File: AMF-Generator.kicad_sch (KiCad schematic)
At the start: 27 parts, among them J1 SW_OUT, J2 CUR_SENSE, J3 PWR_IN, Q1 ISC012N04LM6ATMA1, Q2 ISC012N04LM6ATMA1, U1 ACS732KLATR-75AB, U2 UCC21540

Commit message: initial pass of layout complete
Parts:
- added D3: LED, LED_SMD:LED_0805_2012Metric, symbol Device:LED
- added R9: 2K, Resistor_SMD:R_0805_2012Metric, symbol Device:R
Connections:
- net +12V: now also R9.1
- net GNDPWR: now also D3.1 (K)
- net SW_A: now reaches D1.5, D1.6, D1.7, D1.8, J1.1 (Pin_1), Q1.5 (D), R6.1
- net SW_B: now reaches D2.5, D2.6, D2.7, D2.8, J1.2 (Pin_2), Q2.5 (D), R7.1
- net AC_B: now reaches J2.1 (Pin_1), U1.5 (IP-), U1.6 (IP-), U1.7 (IP-), U1.8 (IP-)
- net AC_A: now reaches J2.2 (Pin_2), U1.1 (IP+), U1.2 (IP+), U1.3 (IP+), U1.4 (IP+)
- net SWA renamed PWM_A
- net SWB renamed PWM_B
- new net: D3.2 (A), R9.2
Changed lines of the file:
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@@
     (effects (font (size 1.27 1.27)) (justify left bottom))
+  )
+  (global_label "AC_A" (shape input) (at 218.44 107.95 90) (fields_autoplaced)
+    (effects (font (size 1.27 1.27)) (justify left))
+    (property "Intersheetrefs" "${INTERSHEET_REFS}" (at 218.44 100.6294 90)
+      (effects (font (size 1.27 1.27)) (justify left) hide)
+    )
+  )
+  (global_label "SW_A" (shape input) (at 175.895 59.69 90) (fields_autoplaced)
+    (effects (font (size 1.27 1.27)) (justify left))
+    (property "Intersheetrefs" "${INTERSHEET_REFS}" (at 175.895 52.0671 90)
+      (effects (font (size 1.27 1.27)) (justify left) hide)
+    )
   )
   (global_label "FAULT" (shape input) (at 274.955 110.49 0) (fields_autoplaced)
@@
     )
   )
-  (global_label "SWA" (shape input) (at 59.69 87.63 180) (fields_autoplaced)
+  (global_label "PWM_A" (shape input) (at 59.69 87.63 180) (fields_autoplaced)
     (effects (font (size 1.27 1.27)) (justify right))
-    (property "Intersheetrefs" "${INTERSHEET_REFS}" (at 53.0347 87.63 0)
+    (property "Intersheetrefs" "${INTERSHEET_REFS}" (at 50.5552 87.63 0)
       (effects (font (size 1.27 1.27)) (justify right) hide)
     )
   )
-  (global_label "SWB" (shape input) (at 59.69 90.17 180) (fields_autoplaced)
+  (global_label "AC_B" (shape input) (at 218.44 113.03 270) (fields_autoplaced)
     (effects (font (size 1.27 1.27)) (justify right))
-    (property "Intersheetrefs" "${INTERSHEET_REFS}" (at 52.8533 90.17 0)
+    (property "Intersheetrefs" "${INTERSHEET_REFS}" (at 218.44 120.532 90)
+      (effects (font (size 1.27 1.27)) (justify right) hide)
+    )
+  )
+  (global_label "PWM_B" (shape input) (at 59.69 90.17 180) (fields_autoplaced)
+    (effects (font (size 1.27 1.27)) (justify right))
+    (property "Intersheetrefs" "${INTERSHEET_REFS}" (at 50.3738 90.17 0)
+      (effects (font (size 1.27 1.27)) (justify right) hide)
+    )
+  )
+  (global_label "SW_B" (shape input) (at 176.53 77.47 270) (fields_autoplaced)
+    (effects (font (size 1.27 1.27)) (justify right))
+    (property "Intersheetrefs" "${INTERSHEET_REFS}" (at 176.53 85.2743 90)
       (effects (font (size 1.27 1.27)) (justify right) hide)
     )
@@
         (path "/c3df021c-646c-4a68-ac14-a081c2121d02"
           (reference "C22") (unit 1)
+        )
+      )
+    )
+  )
+  (symbol (lib_id "power:+12V") (at 31.115 32.385 0) (unit 1)
+    (in_bom yes) (on_board yes) (dnp no) (fields_autoplaced)
+    (property "Reference" "#PWR069" (at 31.115 36.195 0)
+      (effects (font (size 1.27 1.27)) hide)
+    )
+    (property "Value" "+12V" (at 31.115 29.21 0)
+      (effects (font (size 1.27 1.27)))
+    )
+    (property "Footprint" "" (at 31.115 32.385 0)
+      (effects (font (size 1.27 1.27)) hide)
+    )
+    (property "Datasheet" "" (at 31.115 32.385 0)
+      (effects (font (size 1.27 1.27)) hide)
+    )
+    (pin "1")
+    (instances
+      (project "AMF-Generator"
+        (path "/c3df021c-646c-4a68-ac14-a081c2121d02"
+          (reference "#PWR069") (unit 1)
         )
       )
@@
     )
   )
+  (symbol (lib_id "power:GNDPWR") (at 31.115 47.625 0) (unit 1)
+    (in_bom yes) (on_board yes) (dnp no) (fields_autoplaced)
+    (property "Reference" "#PWR068" (at 31.115 52.705 0)
+      (effects (font (size 1.27 1.27)) hide)
+    )
+    (property "Value" "GNDPWR" (at 30.988 52.07 0)
+      (effects (font (size 1.27 1.27)))
+    )
+    (property "Footprint" "" (at 31.115 48.895 0)
+      (effects (font (size 1.27 1.27)) hide)
+    )
+    (property "Datasheet" "" (at 31.115 48.895 0)
+      (effects (font (size 1.27 1.27)) hide)
+    )
+    (pin "1")
+    (instances
+      (project "AMF-Generator"
+        (path "/c3df021c-646c-4a68-ac14-a081c2121d02"
+          (reference "#PWR068") (unit 1)
+        )
+      )
+    )
+  )
   (symbol (lib_id "power:+12V") (at 50.8 39.37 180) (unit 1)
     (in_bom yes) (on_board yes) (dnp no)
@@
         (path "/c3df021c-646c-4a68-ac14-a081c2121d02"
           (reference "C36") (unit 1)
+        )
+      )
+    )
+  )
+  (symbol (lib_id "Device:LED") (at 31.115 43.815 90) (unit 1)
+    (in_bom yes) (on_board yes) (dnp no) (fields_autoplaced)
+    (property "Reference" "D3" (at 34.29 44.7675 90)
+      (effects (font (size 1.27 1.27)) (justify right))
+    )
+    (property "Value" "LED" (at 34.29 47.3075 90)
+      (effects (font (size 1.27 1.27)) (justify right))
+    )
+    (property "Footprint" "LED_SMD:LED_0805_2012Metric" (at 31.115 43.815 0)
+      (effects (font (size 1.27 1.27)) hide)
+    )
+    (property "Datasheet" "~" (at 31.115 43.815 0)
+      (effects (font (size 1.27 1.27)) hide)
+    )
+    (pin "1")
+    (pin "2")
+    (instances
+      (project "AMF-Generator"
+        (path "/c3df021c-646c-4a68-ac14-a081c2121d02"
+          (reference "D3") (unit 1)
         )
       )
@@
         )
       )
+    )
+  )
+  (symbol (lib_id "Device:R") (at 31.115 36.195 0) (unit 1)
+    (in_bom yes) (on_board yes) (dnp no) (fields_autoplaced)
+    (property "Reference" "R9" (at 33.02 35.56 0)
+      (effects (font (size 1.27 1.27)) (justify left))
+    )
+    (property "Value" "2K" (at 33.02 38.1 0)
+      (effects (font (size 1.27 1.27)) (justify left))
+    )
+    (property "Footprint" "Resistor_SMD:R_0805_2012Metric" (at 29.337 36.195 90)
+      (effects (font (size 1.27 1.27)) hide)
+    )
+    (property "Datasheet" "~" (at 31.115 36.195 0)
+      (effects (font (size 1.27 1.27)) hide)
+    )
+    (pin "1")
+    (pin "2")
+    (instances
+      (project "AMF-Generator"
+        (path "/c3df021c-646c-4a68-ac14-a081c2121d02"
+          (reference "R9") (unit 1)
+        )
+      )

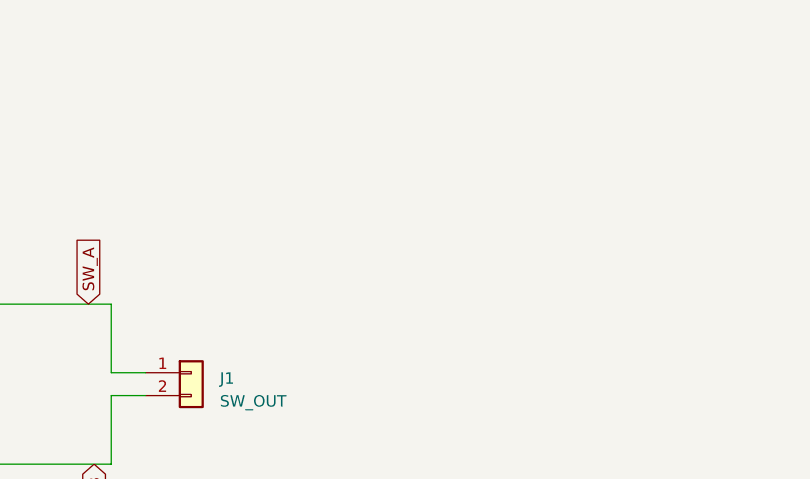
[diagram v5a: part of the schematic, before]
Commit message: Cleanup, changed board outline, DRC errors resolved
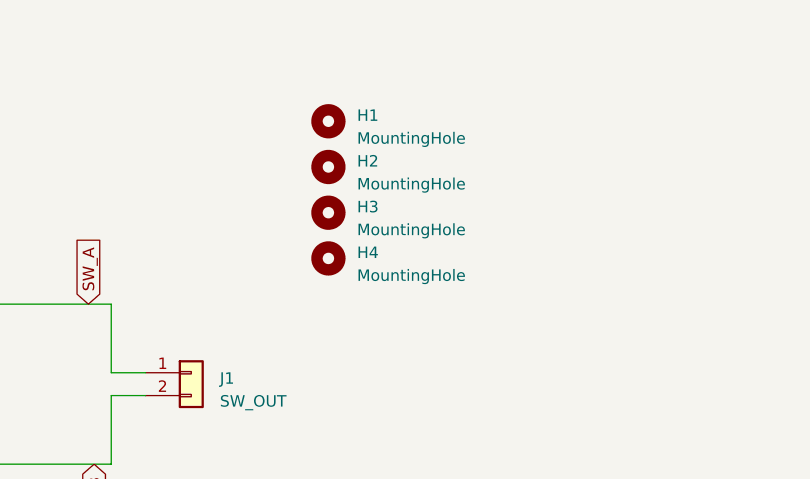
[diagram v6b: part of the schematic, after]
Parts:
- added H1, H2, H3, H4: MountingHole, MountingHole:MountingHole_3.2mm_M3_ISO7380_Pad, symbol Mechanical:MountingHole
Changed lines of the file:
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@@
+    )
+  )
+  (symbol (lib_id "Mechanical:MountingHole") (at 202.565 44.45 0) (unit 1)
+    (in_bom yes) (on_board yes) (dnp no) (fields_autoplaced)
+    (property "Reference" "H2" (at 205.74 43.815 0)
+      (effects (font (size 1.27 1.27)) (justify left))
+    )
+    (property "Value" "MountingHole" (at 205.74 46.355 0)
+      (effects (font (size 1.27 1.27)) (justify left))
+    )
+    (property "Footprint" "MountingHole:MountingHole_3.2mm_M3_ISO7380_Pad" (at 202.565 44.45 0)
+      (effects (font (size 1.27 1.27)) hide)
+    )
+    (property "Datasheet" "~" (at 202.565 44.45 0)
+      (effects (font (size 1.27 1.27)) hide)
+    )
+    (instances
+      (project "AMF-Generator"
+        (path "/c3df021c-646c-4a68-ac14-a081c2121d02"
+          (reference "H2") (unit 1)
+        )
+      )
     )
   )
@@
         (path "/c3df021c-646c-4a68-ac14-a081c2121d02"
           (reference "#PWR015") (unit 1)
+        )
+      )
+    )
+  )
+  (symbol (lib_id "Mechanical:MountingHole") (at 202.565 54.61 0) (unit 1)
+    (in_bom yes) (on_board yes) (dnp no) (fields_autoplaced)
+    (property "Reference" "H4" (at 205.74 53.975 0)
+      (effects (font (size 1.27 1.27)) (justify left))
+    )
+    (property "Value" "MountingHole" (at 205.74 56.515 0)
+      (effects (font (size 1.27 1.27)) (justify left))
+    )
+    (property "Footprint" "MountingHole:MountingHole_3.2mm_M3_ISO7380_Pad" (at 202.565 54.61 0)
+      (effects (font (size 1.27 1.27)) hide)
+    )
+    (property "Datasheet" "~" (at 202.565 54.61 0)
+      (effects (font (size 1.27 1.27)) hide)
+    )
+    (instances
+      (project "AMF-Generator"
+        (path "/c3df021c-646c-4a68-ac14-a081c2121d02"
+          (reference "H4") (unit 1)
         )
       )
@@
         (path "/c3df021c-646c-4a68-ac14-a081c2121d02"
           (reference "#PWR011") (unit 1)
+        )
+      )
+    )
+  )
+  (symbol (lib_id "Mechanical:MountingHole") (at 202.565 39.37 0) (unit 1)
+    (in_bom yes) (on_board yes) (dnp no) (fields_autoplaced)
+    (property "Reference" "H1" (at 205.74 38.735 0)
+      (effects (font (size 1.27 1.27)) (justify left))
+    )
+    (property "Value" "MountingHole" (at 205.74 41.275 0)
+      (effects (font (size 1.27 1.27)) (justify left))
+    )
+    (property "Footprint" "MountingHole:MountingHole_3.2mm_M3_ISO7380_Pad" (at 202.565 39.37 0)
+      (effects (font (size 1.27 1.27)) hide)
+    )
+    (property "Datasheet" "~" (at 202.565 39.37 0)
+      (effects (font (size 1.27 1.27)) hide)
+    )
+    (instances
+      (project "AMF-Generator"
+        (path "/c3df021c-646c-4a68-ac14-a081c2121d02"
+          (reference "H1") (unit 1)
         )
       )
@@
         )
       )
+    )
+  )
+  (symbol (lib_id "Mechanical:MountingHole") (at 202.565 49.53 0) (unit 1)
+    (in_bom yes) (on_board yes) (dnp no) (fields_autoplaced)
+    (property "Reference" "H3" (at 205.74 48.895 0)
+      (effects (font (size 1.27 1.27)) (justify left))
+    )
+    (property "Value" "MountingHole" (at 205.74 51.435 0)
+      (effects (font (size 1.27 1.27)) (justify left))
+    )
+    (property "Footprint" "MountingHole:MountingHole_3.2mm_M3_ISO7380_Pad" (at 202.565 49.53 0)
+      (effects (font (size 1.27 1.27)) hide)
+    )
+    (property "Datasheet" "~" (at 202.565 49.53 0)
+      (effects (font (size 1.27 1.27)) hide)
+    )
+    (instances
+      (project "AMF-Generator"
+        (path "/c3df021c-646c-4a68-ac14-a081c2121d02"
+          (reference "H3") (unit 1)
+        )
+      )

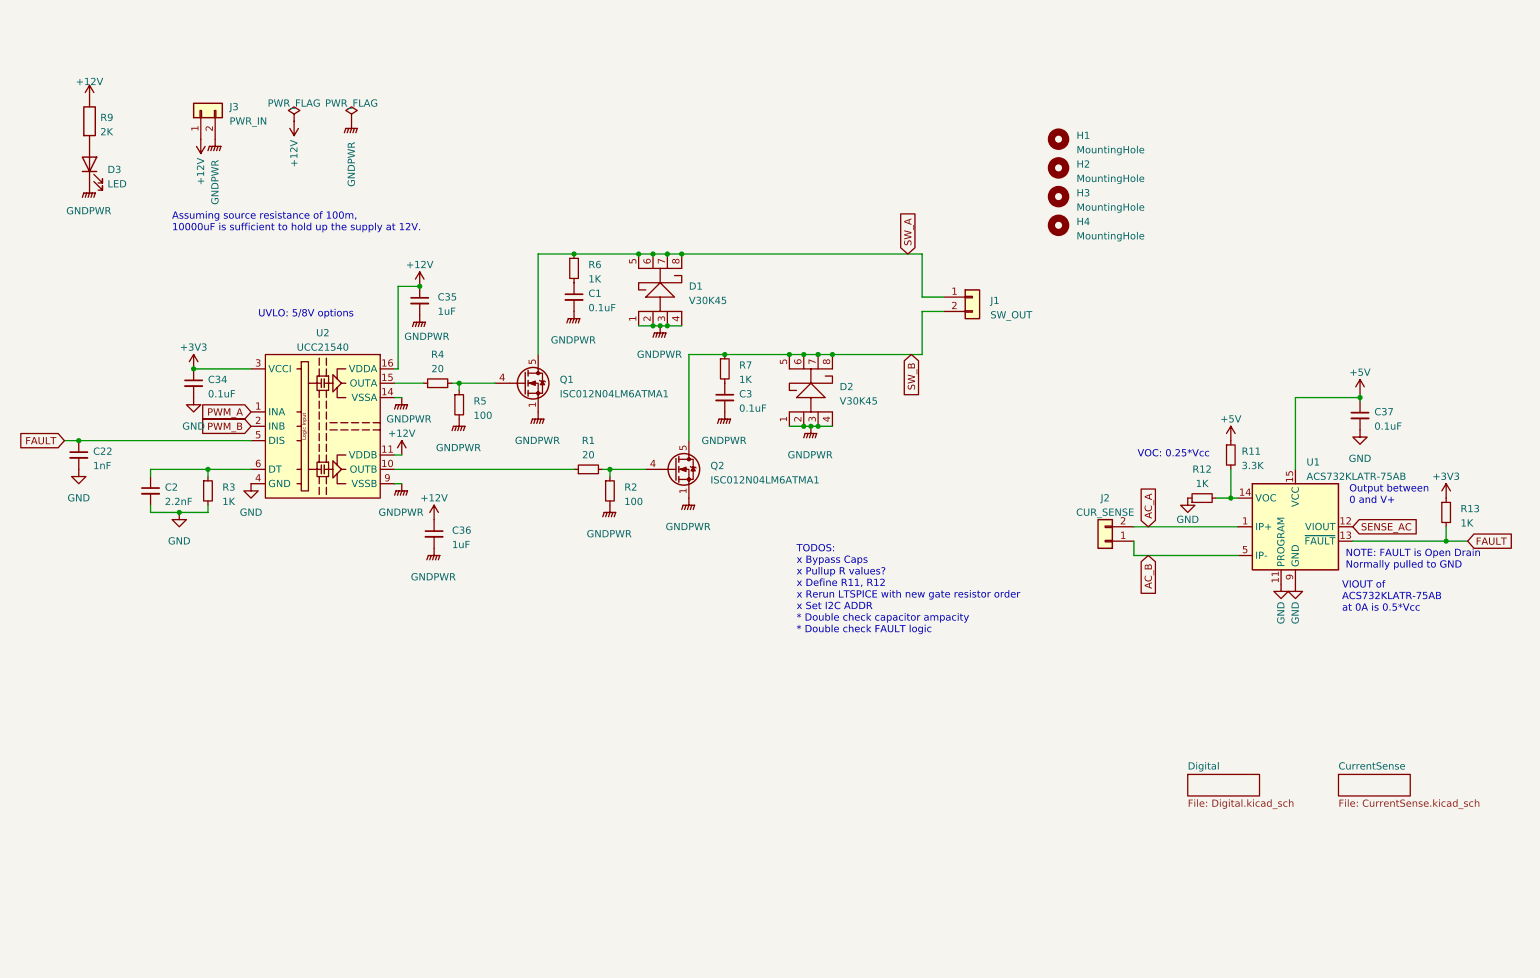
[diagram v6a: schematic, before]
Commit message: Fix schematic issues (incl QTPY symbol) and some board cleanup
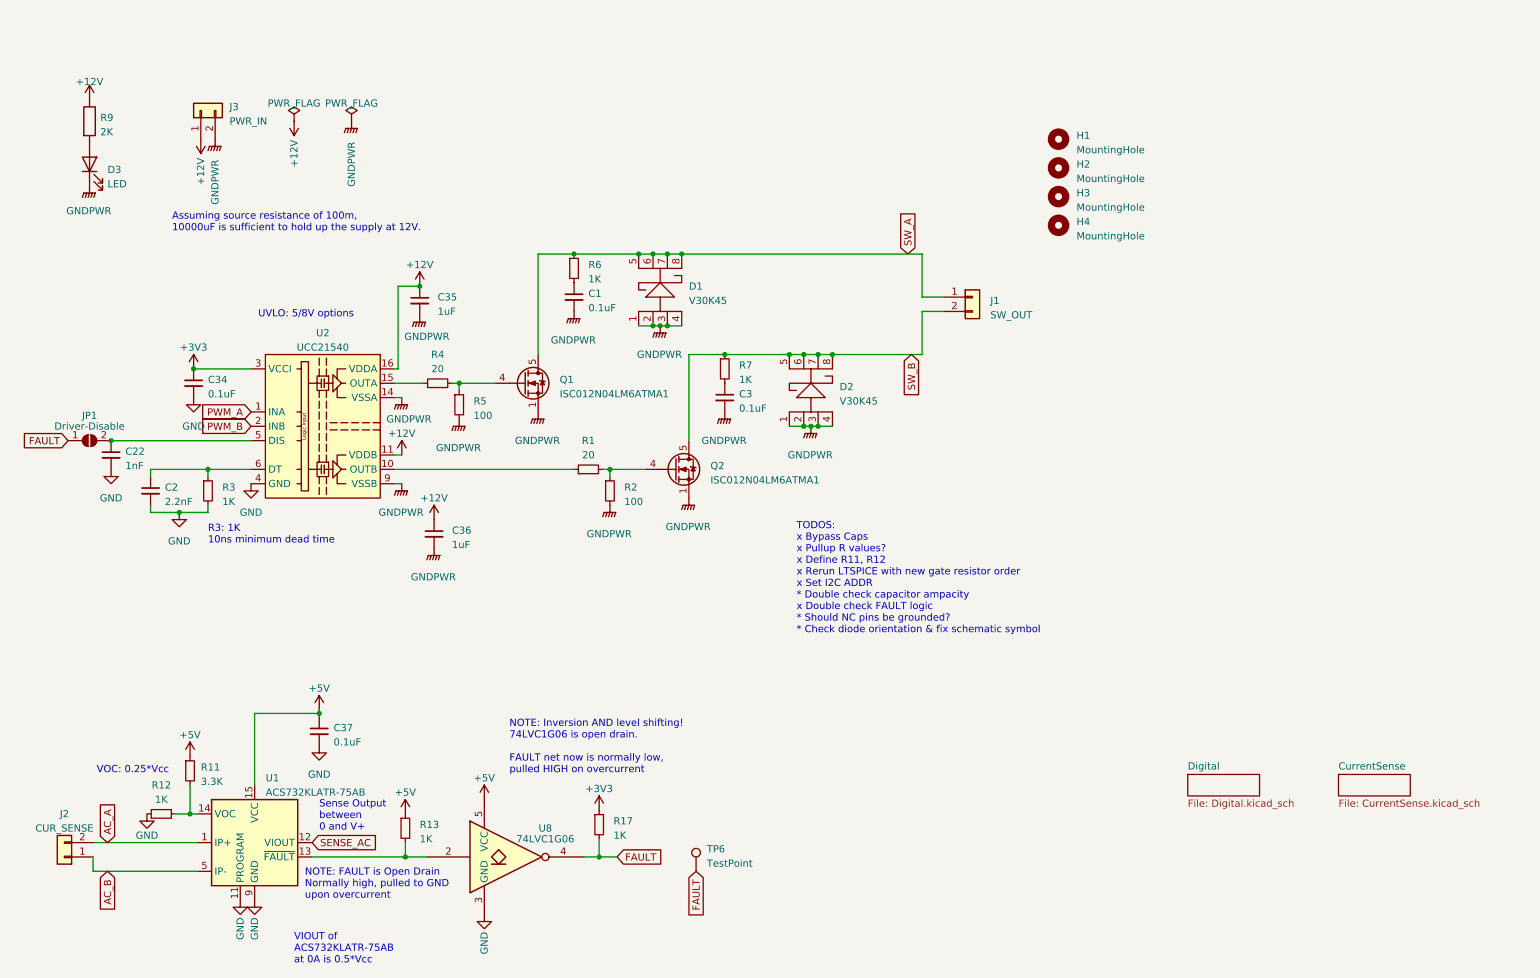
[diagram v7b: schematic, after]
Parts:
- added JP1: Driver-Disable, Jumper:SolderJumper-2_P1.3mm_Open_RoundedPad1.0x1.5mm, symbol Jumper:SolderJumper_2_Open
- added R17: 1K, Resistor_SMD:R_0805_2012Metric, symbol Device:R_Small
- added TP6: TestPoint, TestPoint:TestPoint_THTPad_D2.0mm_Drill1.0mm, symbol Connector:TestPoint
- added U8: 74LVC1G06, Package_TO_SOT_SMD:SOT-23-5_HandSoldering, symbol 74xGxx:74LVC1G06
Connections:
- net +3V3: now also R17.1; no longer R13.1
- net +5V: now also R13.1, U8.5 (VCC)
- net FAULT: now also JP1.1 (A), R17.2, TP6.1, U8.4; no longer C22.1, R13.2, U1.13 (~{FAULT}), U2.5 (DIS)
- net GND: now also U8.3 (GND)
- new net: C22.1, JP1.2 (B), U2.5 (DIS)
- new net: R13.2, U1.13 (~{FAULT}), U8.2
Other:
- note added: "NOTE: FAULT is Open Drain Normally high, pulled to GND upon overcurrent"
- note added: "NOTE: Inversion AND level shifting! 74LVC1G06 is open drain. FAULT net now is normally low, pulled HIGH on overcurrent"
- note added: "R3: 1K 10ns minimum dead time"
- note added: "Sense Output between 0 and V+"
- note added: "TODOS: x Bypass Caps x Pullup R values? x Define R11, R12 x Rerun LTSPICE with new gate resistor order x Set I2C ADDR * Double check capacitor ampacity x Double check FAULT logic * Should NC pins be grounded? * Check diode orientation & fix schematic symbol"
- note removed: "NOTE: FAULT is Open Drain Normally pulled to GND"
- note removed: "Output between 0 and V+"
- note removed: "TODOS: x Bypass Caps x Pullup R values? x Define R11, R12 x Rerun LTSPICE with new gate resistor order x Set I2C ADDR * Double check capacitor ampacity * Double check FAULT logic"
- moved on the sheet: C22, C37, J2, R11, R12, R13, U1

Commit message: misc changes
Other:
- note added: "TODOS: x Bypass Caps x Pullup R values? x Define R11, R12 x Rerun LTSPICE with new gate resistor order x Set I2C ADDR * Double check capacitor ampacity x Double check FAULT logic * Should NC pins be grounded? * Check diode orientation & fix schematic symbol * Calculate appropriate gate resistor value - 20 may be too high"
- note removed: "TODOS: x Bypass Caps x Pullup R values? x Define R11, R12 x Rerun LTSPICE with new gate resistor order x Set I2C ADDR * Double check capacitor ampacity x Double check FAULT logic * Should NC pins be grounded? * Check diode orientation & fix schematic symbol"
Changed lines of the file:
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@@
     (effects (font (size 1.27 1.27)) (justify left bottom))
   )
-  (text "TODOS:\nx Bypass Caps\nx Pullup R values?\nx Define R11, R12\nx Rerun LTSPICE with new gate resistor order\nx Set I2C ADDR\n* Double check capacitor ampacity\nx Double check FAULT logic\n* Should NC pins be grounded?\n* Check diode orientation & fix schematic symbol"
+  (text "TODOS:\nx Bypass Caps\nx Pullup R values?\nx Define R11, R12\nx Rerun LTSPICE with new gate resistor order\nx Set I2C ADDR\n* Double check capacitor ampacity\nx Double check FAULT logic\n* Should NC pins be grounded?\n* Check diode orientation & fix schematic symbol\n* Calculate appropriate gate resistor value - 20 may be too high"
     (at 156.21 127 0)
     (effects (font (size 1.27 1.27)) (justify left bottom))
